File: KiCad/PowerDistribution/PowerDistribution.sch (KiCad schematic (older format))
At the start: 10 parts, among them SW1 ChangeoverSwitch

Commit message: Updated KiCad Schematics
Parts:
- removed R1: 11.3V Load_1, symbol Device:R_US
- removed R2: 22.2V Load_1, symbol Device:R_US
- removed R3: 11.3V Load_SW, symbol Device:R_US
- removed R4: 22.2V Load_SW, symbol Device:R_US
- removed R5: 11.3V Load_2, symbol Device:R_US
- removed R6: 22.2V Load_2, symbol Device:R_US
- added F1, F2, F3, F7, F8, F9: 3A, symbol Device:Fuse
- added F4: 10A, symbol Device:Fuse
- added F6: 7.5A, symbol Device:Fuse
- added U1, U2: FuseBlock, symbol RoboBoat_Parts:FuseBlock
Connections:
- net 0: no longer SW1.5, SW1.7
- net at SW1.6, SW1.8: now also U1.2 (-MAIN), U2.2 (-MAIN)
- net at SW1.2, SW1.4: now also U1.1 (+MAIN)
- net at SW1.10, SW1.12: now also U2.1 (+MAIN)
- new net: F6.1, U2.~
- new net: F6.2, U2.~
- new net: F7.1, U2.~
- new net: F7.2, U2.~
- new net: F8.1, U2.~
- new net: F8.2, U2.~
- new net: F4.1, U1.~
- new net: F4.2, U1.~
- new net: F9.1, U1.~
- new net: F9.2, U1.~
- new net: F1.1, U1.~
- new net: F1.2, U1.~
- new net: F2.1, U1.~
- new net: F2.2, U1.~
- new net: F3.1, U1.~
- new net: F3.2, U1.~
- new net FeatherPower: U2.10 (+)
- new net GL-iNet: U1.10 (+)
- new net GND: SW1.5, SW1.7
- new net MotorRelay: U2.11 (+)
- new net RPi: U1.11 (+)
- new net StatusLights: U2.9 (+)
- new net TP-Link: U1.9 (+)
- new net TX2: U1.12 (+)
- new net USB_Hub: U1.13 (+)
- no-connect marks 1 -> 13
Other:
- note added: "Simulated Sources\n"
- note removed: "Simulation Switch Setting 1"
- note removed: "Simulation Switch Setting 2"
- moved on the sheet: SW1, V1, V2, V3

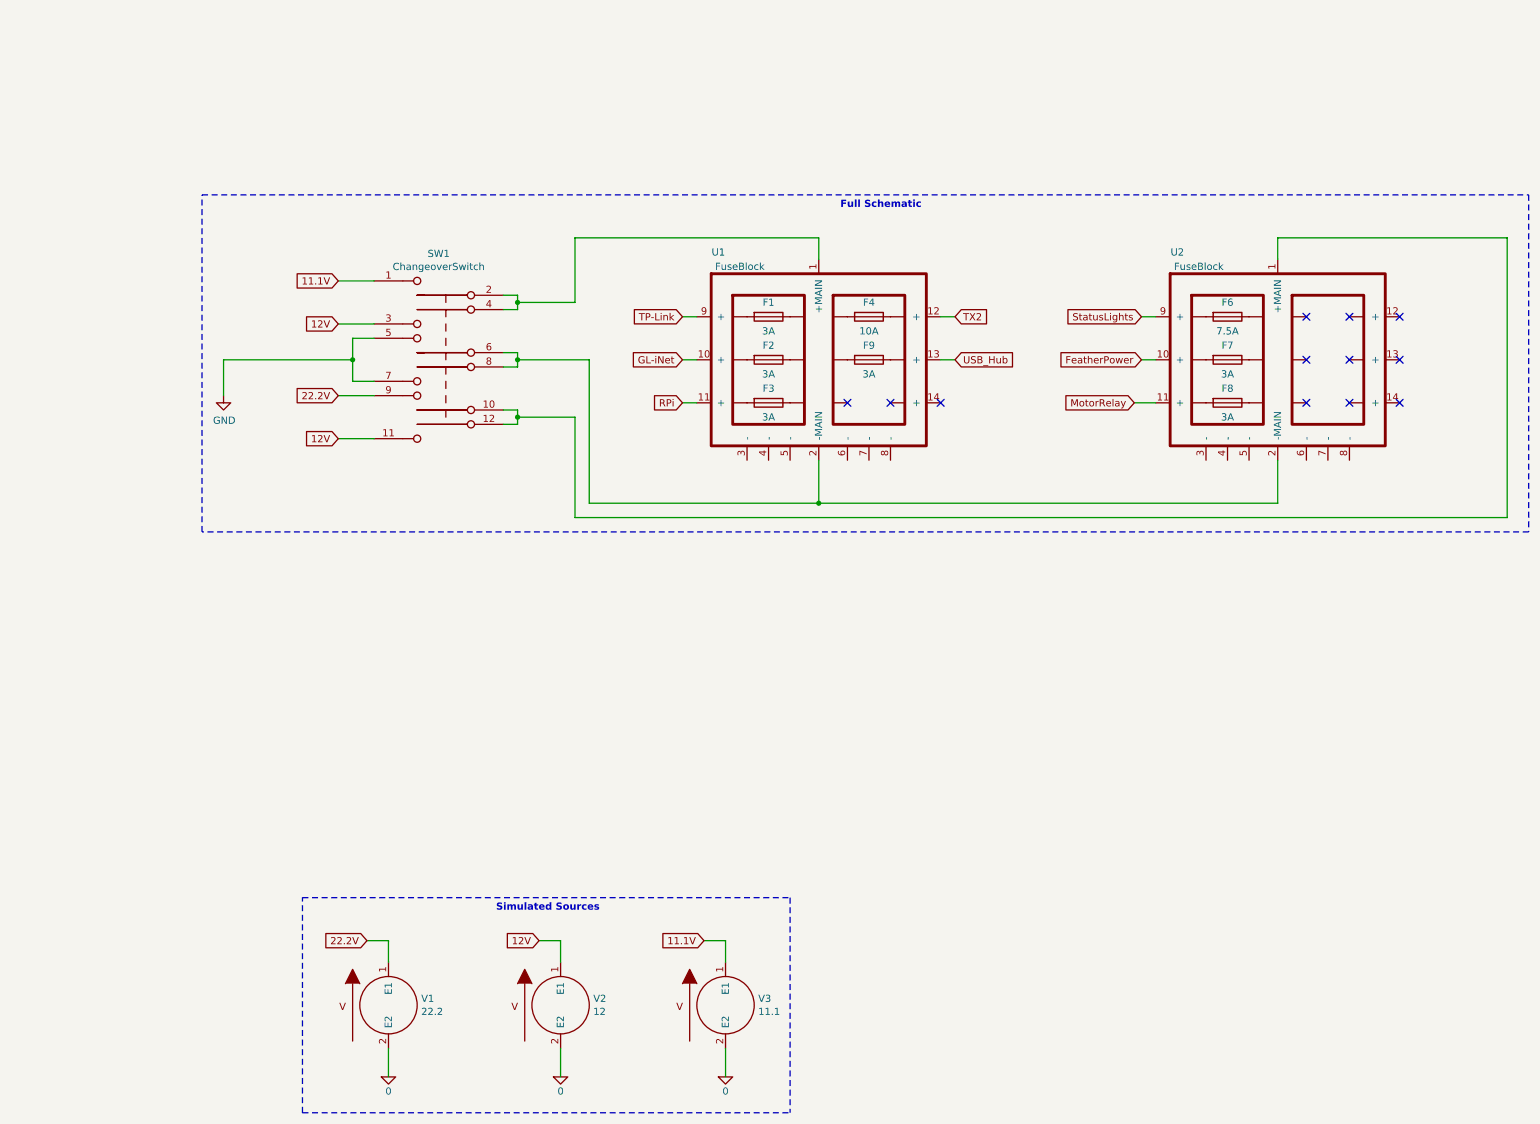
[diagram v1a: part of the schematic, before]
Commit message: Updated the power distribution schematic
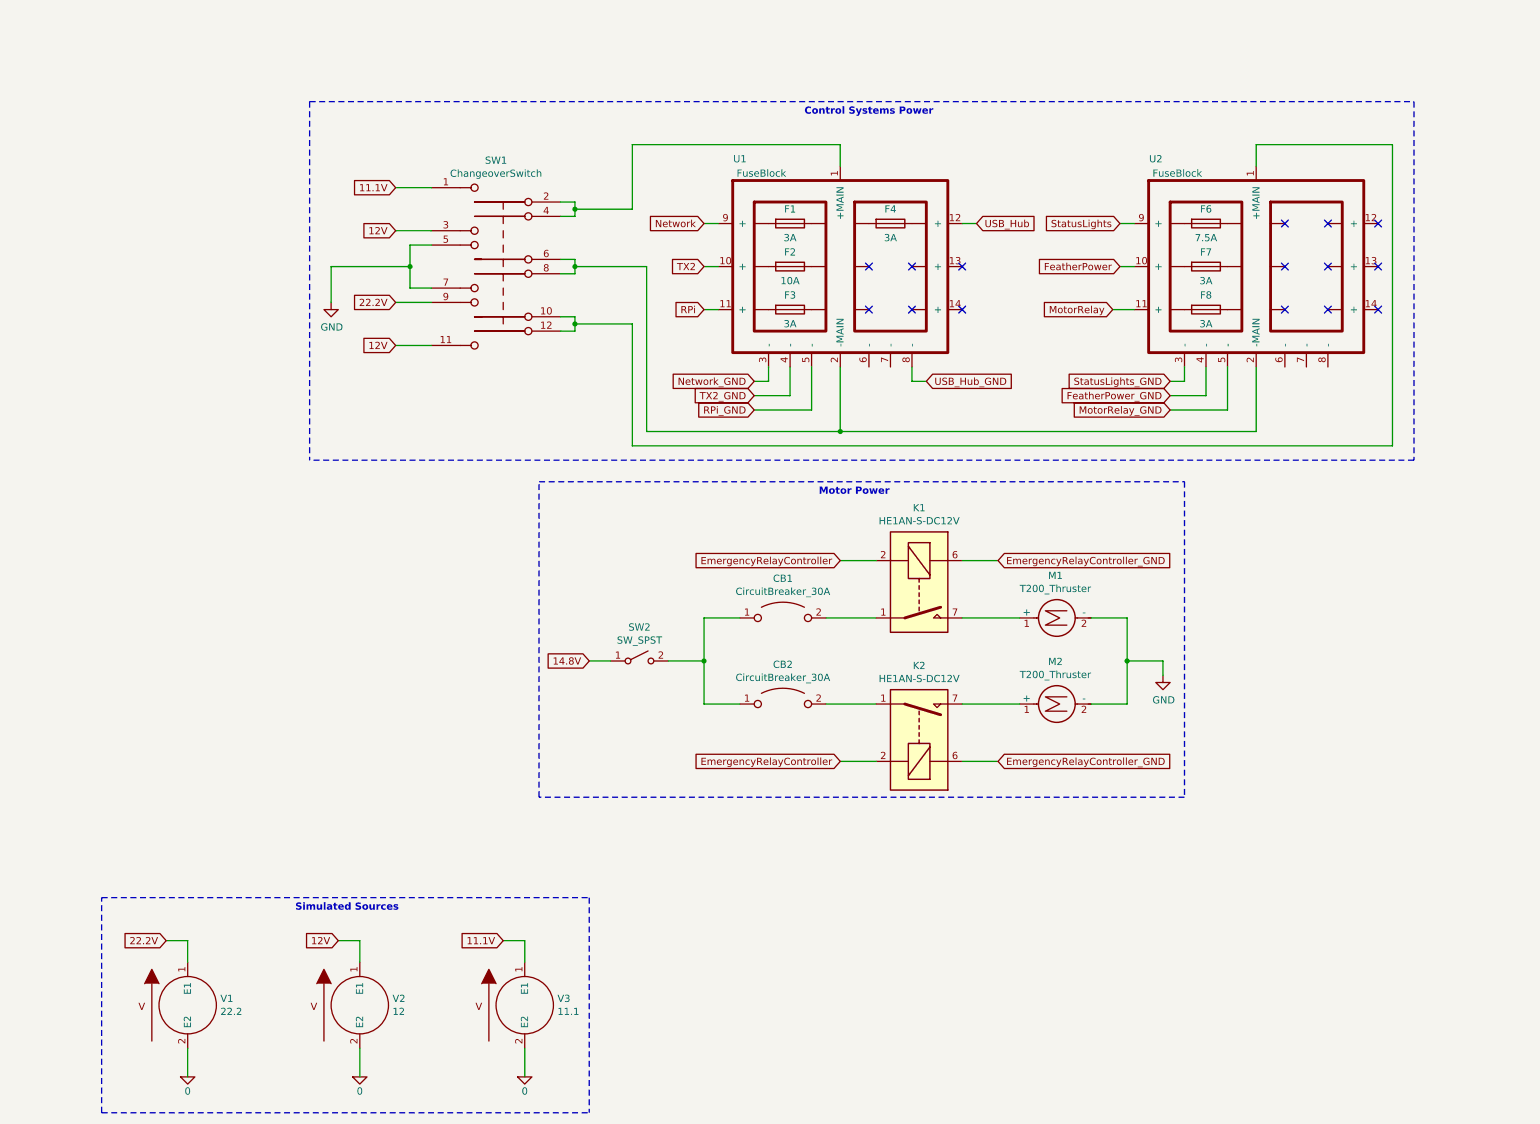
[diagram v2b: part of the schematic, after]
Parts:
- removed F9: 3A, symbol Device:Fuse
- added CB1, CB2: CircuitBreaker_30A, symbol Device:CircuitBreaker_1P_US
- added K1, K2: HE1AN-S-DC12V, Relay_THT:Relay_StandexMeder_DIP_LowProfile, symbol Relay:DIPxx-1Axx-11x
- added M1, M2: T200_Thruster, symbol Motor:Motor_DC
- added SW2: SW_SPST, symbol Switch:SW_SPST
- F2: value 3A -> 10A
- F4: value 10A -> 3A
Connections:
- net GL-iNet is gone; now on net TX2: U1.10 (+)
- net GND: now also M1.2 (-), M2.2 (-)
- net TX2: no longer U1.12 (+)
- net USB_Hub: now also U1.12 (+); no longer U1.13 (+)
- net StatusLights_GND: now reaches U2.3 (-)
- net FeatherPower_GND: now reaches U2.4 (-)
- net MotorRelay_GND: now reaches U2.5 (-)
- net at U2.~: now also F8.2
- net at U1.~: now also F3.2
- net Network_GND: now reaches U1.3 (-)
- net TX2_GND: now reaches U1.4 (-)
- net RPi_GND: now reaches U1.5 (-)
- net USB_Hub_GND: now reaches U1.8 (-)
- net TP-Link renamed Network
- new net: CB1.1, CB2.1, SW2.2 (B)
- new net: CB1.2, K1.1, K1.14
- new net: CB2.2, K2.1, K2.14
- new net: K1.7, K1.8, M1.1 (+)
- new net: K2.7, K2.8, M2.1 (+)
- new net 14.8V: SW2.1 (A)
- new net EmergencyRelayController: K1.2, K2.2
- new net EmergencyRelayController_GND: K1.6, K2.6
- no-connect marks 13 -> 16
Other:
- note added: "Control Systems Power"
- note added: "Motor Power"
- note removed: "Full Schematic"
- moved on the sheet: F1, F2, F3, F4, F6, F7, F8, SW1, U1, U2, V1, V2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
